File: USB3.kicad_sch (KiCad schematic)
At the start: 12 parts, among them J1901 USB_C_Receptacle, J1902 USB_C_Receptacle, U1902 AP22653W6-7

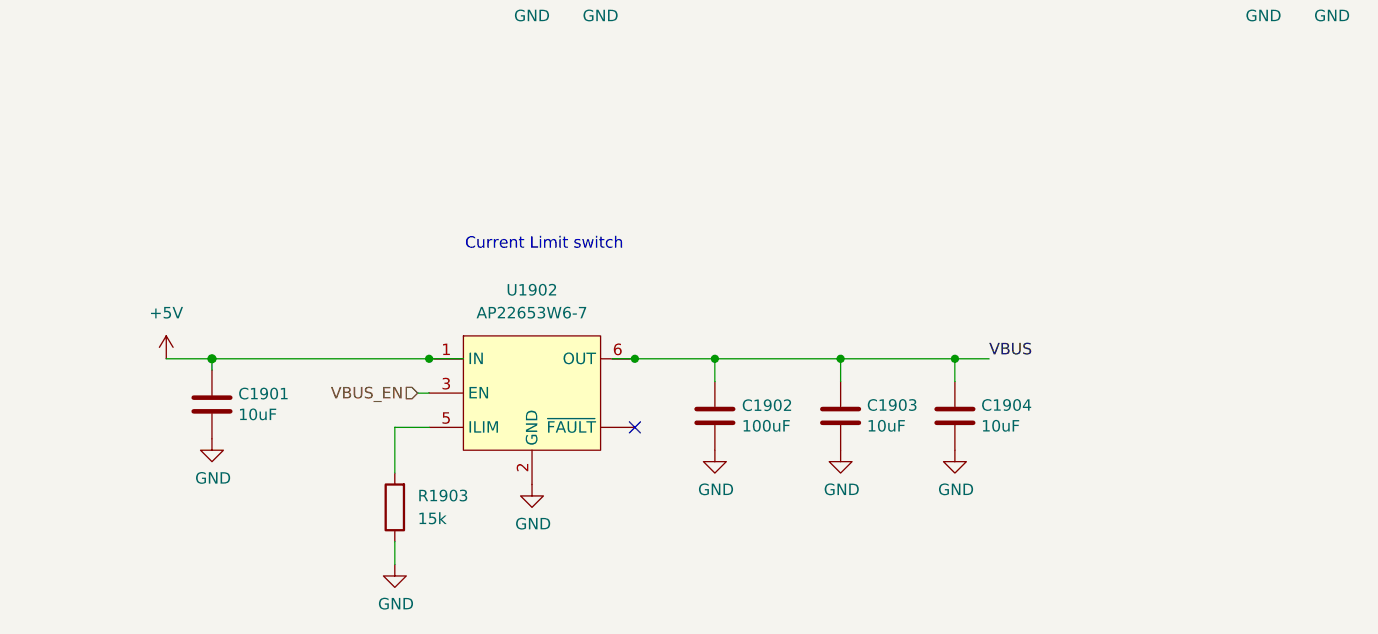
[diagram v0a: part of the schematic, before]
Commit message: Implement ideal diodes for input and LDO power ORing
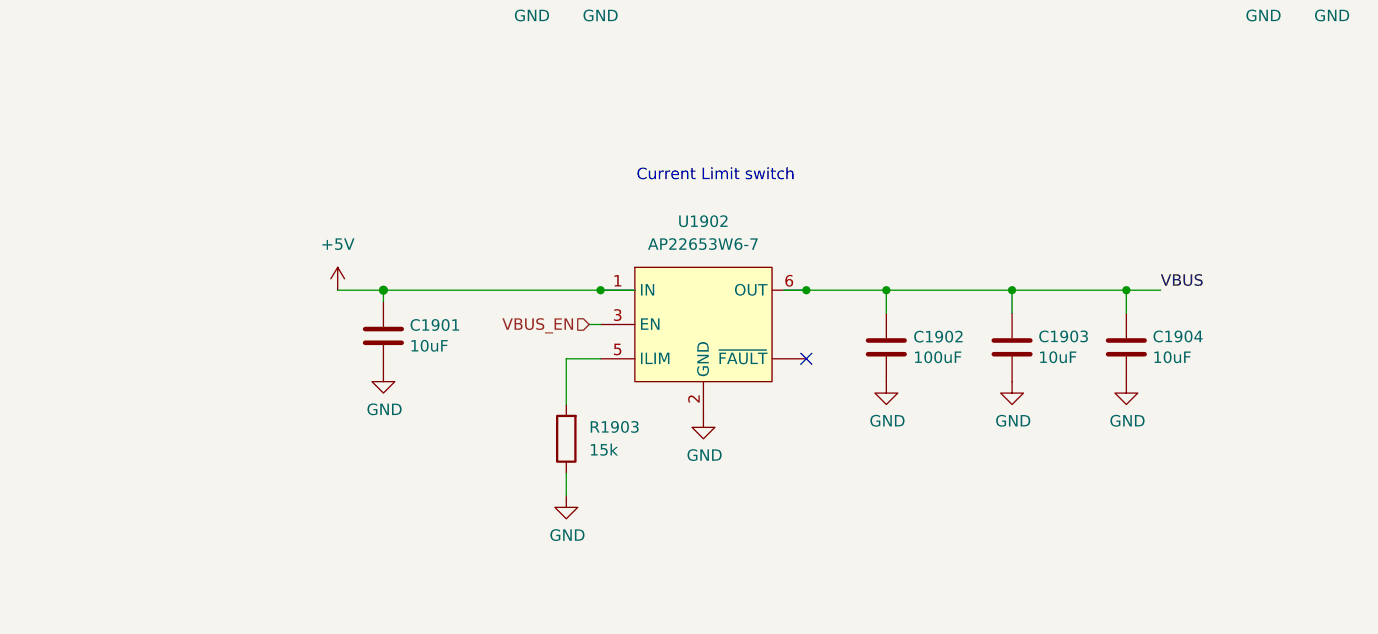
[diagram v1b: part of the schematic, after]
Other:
- moved on the sheet: C1901, C1902, C1903, C1904, R1903, U1902

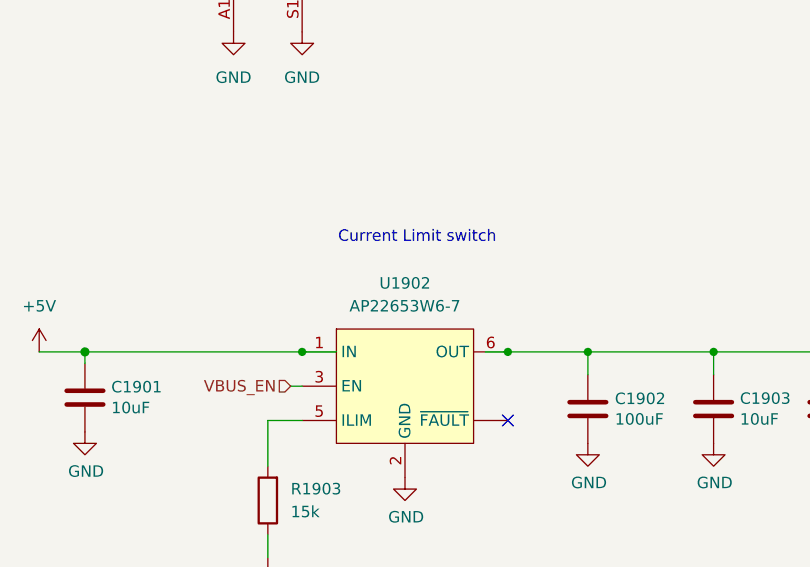
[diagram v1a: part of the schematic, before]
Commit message: Re-annotate schematics
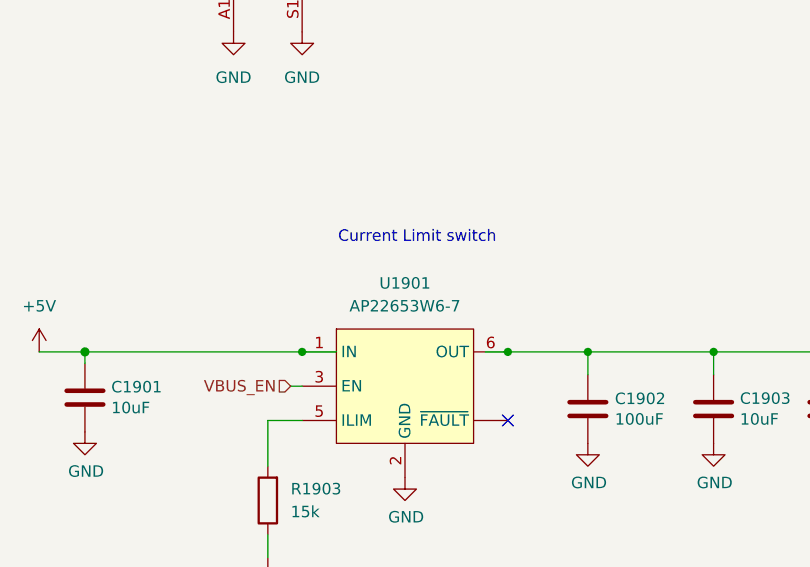
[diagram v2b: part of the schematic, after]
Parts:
- renumbered U1902 to U1901
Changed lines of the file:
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@@
-			)
-		)
-		(property "Sim.Enable" ""
-			(at 72.39 43.18 0)
-			(effects
-				(font
-					(size 1.27 1.27)
-				)
-				(hide yes)
 			)
 		)
@@
 			)
 		)
-		(property "Sim.Enable" ""
-			(at 78.74 160.02 0)
-			(effects
-				(font
-					(size 1.27 1.27)
-				)
-				(hide yes)
-			)
-		)
 		(pin "1"
 		)
@@
 		(on_board yes)
 		(dnp no)
-		(property "Reference" "#PWR01905"
+		(property "Reference" "#PWR01908"
 			(at 114.3 175.26 0)
 			(effects
@@
 			(project "HALPI2"
 				(path "/abc482bd-3f17-4d35-80db-1da3dcdb5c27/b774f543-305e-4249-92c3-c3de7e8a285e"
-					(reference "#PWR01905")
+					(reference "#PWR01908")
 					(unit 1)
 				)
@@
 		(dnp no)
 		(fields_autoplaced yes)
-		(property "Reference" "#PWR01903"
+		(property "Reference" "#PWR01901"
 			(at 67.31 44.45 0)
 			(effects
@@
 			(project "HALPI2"
 				(path "/abc482bd-3f17-4d35-80db-1da3dcdb5c27/b774f543-305e-4249-92c3-c3de7e8a285e"
-					(reference "#PWR01903")
+					(reference "#PWR01901")
 					(unit 1)
 				)
@@
 		(dnp no)
 		(fields_autoplaced yes)
-		(property "Reference" "#PWR01901"
+		(property "Reference" "#PWR01903"
 			(at 73.66 158.75 0)
 			(effects
@@
 			(project ""
 				(path "/abc482bd-3f17-4d35-80db-1da3dcdb5c27/b774f543-305e-4249-92c3-c3de7e8a285e"
-					(reference "#PWR01901")
+					(reference "#PWR01903")
 					(unit 1)
 				)
@@
 		(on_board yes)
 		(dnp no)
-		(property "Reference" "#PWR01912"
+		(property "Reference" "#PWR01913"
 			(at 161.29 171.45 0)
 			(effects
@@
 			(project "HALPI2"
 				(path "/abc482bd-3f17-4d35-80db-1da3dcdb5c27/b774f543-305e-4249-92c3-c3de7e8a285e"
-					(reference "#PWR01912")
+					(reference "#PWR01913")
 					(unit 1)
 				)
@@
 			)
 		)
-		(property "Sim.Enable" ""
-			(at 153.67 43.18 0)
-			(effects
-				(font
-					(size 1.27 1.27)
-				)
-				(hide yes)
-			)
-		)
 		(pin "2"
 		)
@@
 			)
 		)
-		(property "Sim.Enable" ""
-			(at 99.06 171.45 0)
-			(effects
-				(font
-					(size 1.27 1.27)
-				)
-				(hide yes)
-			)
-		)
 		(pin "1"
 		)
@@
 		(on_board yes)
 		(dnp no)
-		(property "Reference" "#PWR01910"
+		(property "Reference" "#PWR01911"
 			(at 148.59 171.45 0)
 			(effects
@@
 			(project "HALPI2"
 				(path "/abc482bd-3f17-4d35-80db-1da3dcdb5c27/b774f543-305e-4249-92c3-c3de7e8a285e"
-					(reference "#PWR01910")
+					(reference "#PWR01911")
 					(unit 1)
 				)
@@
 		)
 		(property "LCSC" "C15850"
-			(at 161.29 161.29 0)
-			(effects
-				(font
-					(size 1.27 1.27)
-				)
-				(hide yes)
-			)
-		)
-		(property "Sim.Enable" ""
 			(at 161.29 161.29 0)
 			(effects
@@
 			)
 		)
-		(property "Sim.Enable" ""
-			(at 148.59 43.18 0)
-			(effects
-				(font
-					(size 1.27 1.27)
-				)
-				(hide yes)
-			)
-		)
 		(pin "2"
 		)
@@
 			)
 		)
-		(property "Sim.Enable" ""
-			(at 67.31 43.18 0)
-			(effects
-				(font
-					(size 1.27 1.27)
-				)
-				(hide yes)
-			)
-		)
 		(pin "2"
 		)
@@
 			)
 		)
-		(property "Sim.Enable" ""
-			(at 95.25 78.74 0)
-			(effects
-				(font
-					(size 1.27 1.27)
-				)
-				(hide yes)
-			)
-		)
 		(pin "A12"
 		)
@@
 		(dnp no)
 		(fields_autoplaced yes)
-		(property "Reference" "#PWR01913"
+		(property "Reference" "#PWR01912"
 			(at 153.67 44.45 0)
 			(effects
@@
 			(project ""
 				(path "/abc482bd-3f17-4d35-80db-1da3dcdb5c27/b774f543-305e-4249-92c3-c3de7e8a285e"
-					(reference "#PWR01913")
+					(reference "#PWR01912")
 					(unit 1)
 				)
@@
 		(on_board yes)
 		(dnp no)
-		(property "Reference" "#PWR01908"
+		(property "Reference" "#PWR01906"
 			(at 99.06 184.15 0)
 			(effects
@@
 			(project "HALPI2"
 				(path "/abc482bd-3f17-4d35-80db-1da3dcdb5c27/b774f543-305e-4249-92c3-c3de7e8a285e"
-					(reference "#PWR01908")
+					(reference "#PWR01906")
 					(unit 1)
 				)
@@
 		(dnp no)
 		(fields_autoplaced yes)
-		(property "Reference" "#PWR01906"
+		(property "Reference" "#PWR01905"
 			(at 95.25 125.73 0)
 			(effects
@@
 			(project ""
 				(path "/abc482bd-3f17-4d35-80db-1da3dcdb5c27/b774f543-305e-4249-92c3-c3de7e8a285e"
-					(reference "#PWR01906")
+					(reference "#PWR01905")
 					(unit 1)
 				)
@@
 			)
 		)
-		(property "Sim.Enable" ""
-			(at 148.59 161.29 0)
-			(effects
-				(font
-					(size 1.27 1.27)
-				)
-				(hide yes)
-			)
-		)
 		(pin "1"
 		)
@@
 		(dnp no)
 		(fields_autoplaced yes)
-		(property "Reference" "U1902"
+		(property "Reference" "U1901"
 			(at 114.3 147.32 0)
 			(effects
@@
 			)
 		)
-		(property "Sim.Enable" ""
-			(at 114.3 158.75 0)
-			(effects
-				(font
-					(size 1.27 1.27)
-				)
-				(hide yes)
-			)
-		)
 		(pin ""
 		)
@@
 			(project ""
 				(path "/abc482bd-3f17-4d35-80db-1da3dcdb5c27/b774f543-305e-4249-92c3-c3de7e8a285e"
-					(reference "U1902")
+					(reference "U1901")
 					(unit 1)
 				)
@@
 		(dnp no)
 		(fields_autoplaced yes)
-		(property "Reference" "#PWR01911"
+		(property "Reference" "#PWR01910"
 			(at 148.59 44.45 0)
 			(effects
@@
 			(project "HALPI2"
 				(path "/abc482bd-3f17-4d35-80db-1da3dcdb5c27/b774f543-305e-4249-92c3-c3de7e8a285e"
-					(reference "#PWR01911")
+					(reference "#PWR01910")
 					(unit 1)
 				)
@@
 			)
 		)
-		(property "Sim.Enable" ""
-			(at 134.62 161.29 0)
-			(effects
-				(font
-					(size 1.27 1.27)
-				)
-				(hide yes)
-			)
-		)
 		(pin "1"
 		)
@@
 		(on_board yes)
 		(dnp no)
-		(property "Reference" "#PWR01902"
+		(property "Reference" "#PWR01904"
 			(at 78.74 170.18 0)
 			(effects
@@
 			(project "HALPI2"
 				(path "/abc482bd-3f17-4d35-80db-1da3dcdb5c27/b774f543-305e-4249-92c3-c3de7e8a285e"
-					(reference "#PWR01902")
+					(reference "#PWR01904")
 					(unit 1)
 				)
@@
 		(dnp no)
 		(fields_autoplaced yes)
-		(property "Reference" "#PWR01904"
+		(property "Reference" "#PWR01902"
 			(at 72.39 44.45 0)
 			(effects
@@
 			(project "HALPI2"
 				(path "/abc482bd-3f17-4d35-80db-1da3dcdb5c27/b774f543-305e-4249-92c3-c3de7e8a285e"
-					(reference "#PWR01904")
+					(reference "#PWR01902")
 					(unit 1)
 				)
@@
 			(at 176.53 78.74 0)
 			(effects
-				(font
-					(size 1.27 1.27)
-				)
-				(hide yes)
-			)
-		)
-		(property "Sim.Enable" ""
-			(at 176.53 78.74 0)
-			(effects

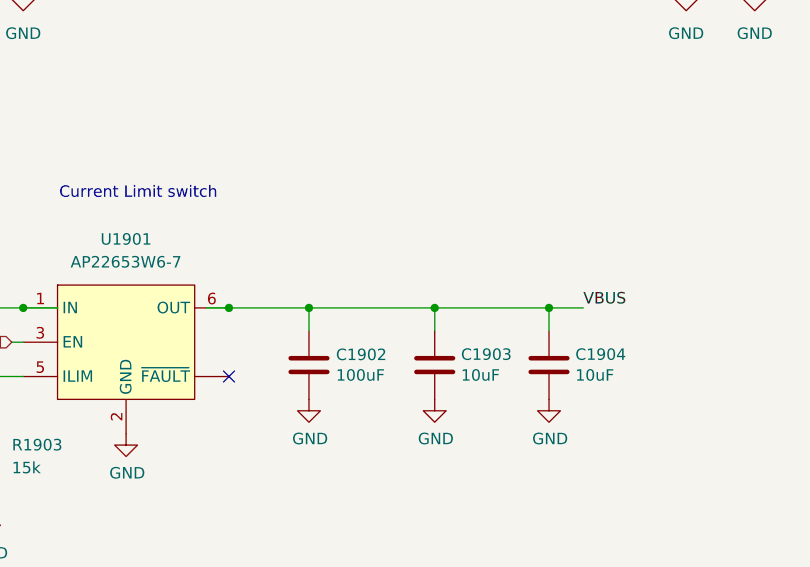
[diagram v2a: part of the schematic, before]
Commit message: Sprinkle test points on the schematics
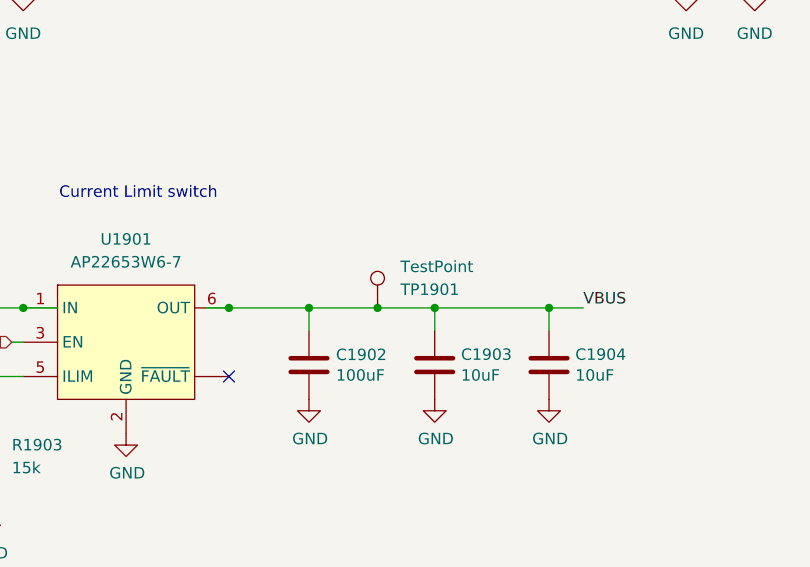
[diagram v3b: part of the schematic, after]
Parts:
- added TP1901: TestPoint, TestPoint:TestPoint_Pad_D1.0mm, symbol Connector:TestPoint
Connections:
- net VBUS: now also TP1901.1
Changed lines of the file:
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@@
 	)
 	(junction
+		(at 142.24 154.94)
+		(diameter 0)
+		(color 0 0 0 0)
+	)
+	(junction
 		(at 148.59 154.94)
 		(diameter 0)
@@
 	(wire
 		(pts
+			(xy 142.24 154.94) (xy 148.59 154.94)
+		)
+		(stroke
+			(width 0)
+			(type solid)
+		)
+	)
+	(wire
+		(pts
 			(xy 139.7 93.98) (xy 161.29 93.98)
 		)
@@
 	(wire
 		(pts
-			(xy 134.62 154.94) (xy 148.59 154.94)
+			(xy 134.62 154.94) (xy 142.24 154.94)
 		)
 		(stroke
@@
 			)
 		)
+		(property "Sim.Enable" ""
+			(at 72.39 43.18 0)
+			(effects
+				(font
+					(size 1.27 1.27)
+				)
+				(hide yes)
+			)
+		)
 		(pin "2"
 		)
@@
 			)
 		)
+		(property "Sim.Enable" ""
+			(at 78.74 160.02 0)
+			(effects
+				(font
+					(size 1.27 1.27)
+				)
+				(hide yes)
+			)
+		)
 		(pin "1"
 		)
@@
 			)
 		)
+		(property "Sim.Enable" ""
+			(at 153.67 43.18 0)
+			(effects
+				(font
+					(size 1.27 1.27)
+				)
+				(hide yes)
+			)
+		)
 		(pin "2"
 		)
@@
 			)
 		)
+		(property "Sim.Enable" ""
+			(at 99.06 171.45 0)
+			(effects
+				(font
+					(size 1.27 1.27)
+				)
+				(hide yes)
+			)
+		)
 		(pin "1"
 		)
@@
 			)
 		)
+		(property "Sim.Enable" ""
+			(at 161.29 161.29 0)
+			(effects
+				(font
+					(size 1.27 1.27)
+				)
+				(hide yes)
+			)
+		)
 		(pin "1"
 		)
@@
 			)
 		)
+		(property "Sim.Enable" ""
+			(at 148.59 43.18 0)
+			(effects
+				(font
+					(size 1.27 1.27)
+				)
+				(hide yes)
+			)
+		)
 		(pin "2"
 		)
@@
 			)
 		)
+		(property "Sim.Enable" ""
+			(at 67.31 43.18 0)
+			(effects
+				(font
+					(size 1.27 1.27)
+				)
+				(hide yes)
+			)
+		)
 		(pin "2"
 		)
@@
 			)
 		)
+		(property "Sim.Enable" ""
+			(at 95.25 78.74 0)
+			(effects
+				(font
+					(size 1.27 1.27)
+				)
+				(hide yes)
+			)
+		)
 		(pin "A12"
 		)
@@
 	)
 	(symbol
+		(lib_id "Connector:TestPoint")
+		(at 142.24 154.94 0)
+		(mirror y)
+		(unit 1)
+		(exclude_from_sim no)
+		(in_bom yes)
+		(on_board yes)
+		(dnp no)
+		(property "Reference" "TP1901"
+			(at 144.78 152.9081 0)
+			(effects
+				(font
+					(size 1.27 1.27)
+				)
+				(justify right)
+			)
+		)
+		(property "Value" "TestPoint"
+			(at 144.78 150.3681 0)
+			(effects
+				(font
+					(size 1.27 1.27)
+				)
+				(justify right)
+			)
+		)
+		(property "Footprint" "TestPoint:TestPoint_Pad_D1.0mm"
+			(at 137.16 154.94 0)
+			(effects
+				(font
+					(size 1.27 1.27)
+				)
+				(hide yes)
+			)
+		)
+		(property "Datasheet" "~"
+			(at 137.16 154.94 0)
+			(effects
+				(font
+					(size 1.27 1.27)
+				)
+				(hide yes)
+			)
+		)
+		(property "Description" "test point"
+			(at 142.24 154.94 0)
+			(effects
+				(font
+					(size 1.27 1.27)
+				)
+				(hide yes)
+			)
+		)
+		(pin "1"
+		)
+		(instances
+			(project "HALPI2"
+				(path "/abc482bd-3f17-4d35-80db-1da3dcdb5c27/b774f543-305e-4249-92c3-c3de7e8a285e"
+					(reference "TP1901")
+					(unit 1)
+				)
+			)
+		)
+	)
+	(symbol
 		(lib_id "power:GND")
 		(at 95.25 119.38 0)
@@
 			)
 		)
+		(property "Sim.Enable" ""
+			(at 148.59 161.29 0)
+			(effects
+				(font
+					(size 1.27 1.27)
+				)
+				(hide yes)
+			)
+		)
 		(pin "1"
 		)
@@
 			)
 		)
+		(property "Sim.Enable" ""
+			(at 114.3 158.75 0)
+			(effects
+				(font
+					(size 1.27 1.27)
+				)
+				(hide yes)
+			)
+		)
 		(pin ""
 		)
@@
 			)
 		)
+		(property "Sim.Enable" ""
+			(at 134.62 161.29 0)
+			(effects
+				(font
+					(size 1.27 1.27)
+				)
+				(hide yes)
+			)
+		)
 		(pin "1"
 		)
@@
 			(at 176.53 78.74 0)
 			(effects
+				(font
+					(size 1.27 1.27)
+				)
+				(hide yes)
+			)
+		)
+		(property "Sim.Enable" ""
+			(at 176.53 78.74 0)
+			(effects
